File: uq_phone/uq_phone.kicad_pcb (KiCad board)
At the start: 2 copper layers, 113.5 x 110.8 mm, 151 parts, among them J1 USB4105-GF-A, J10 Conn_01x02, J2 S3B-PH-SM4-TB_LF__SN_, J3 20279-001E-03, J4 20279-001E-03, J5 0786463001, J6 503398-1892, J7 Conn_01x02, J8 54132-4062, J9 SJ-3551B-MSMT-TR-67, Q1 MMBT3904, Q2 MMBT3904, Q3 MMBT2907ALT1G, U1 MCP73871-2CCI_ML, U10 TS3A5018RSVR, U11 NAU88C22YG, U2 TPS62162DSGR, U3 BQ27441DRZR-G1A, U4 RC7620_1104625, U5 TXB0108RGYR, U6 TXB0108RGYR, U7 STM32H730VBTx, U8 LSM6DSVTR, U9 DRV2603RUNR

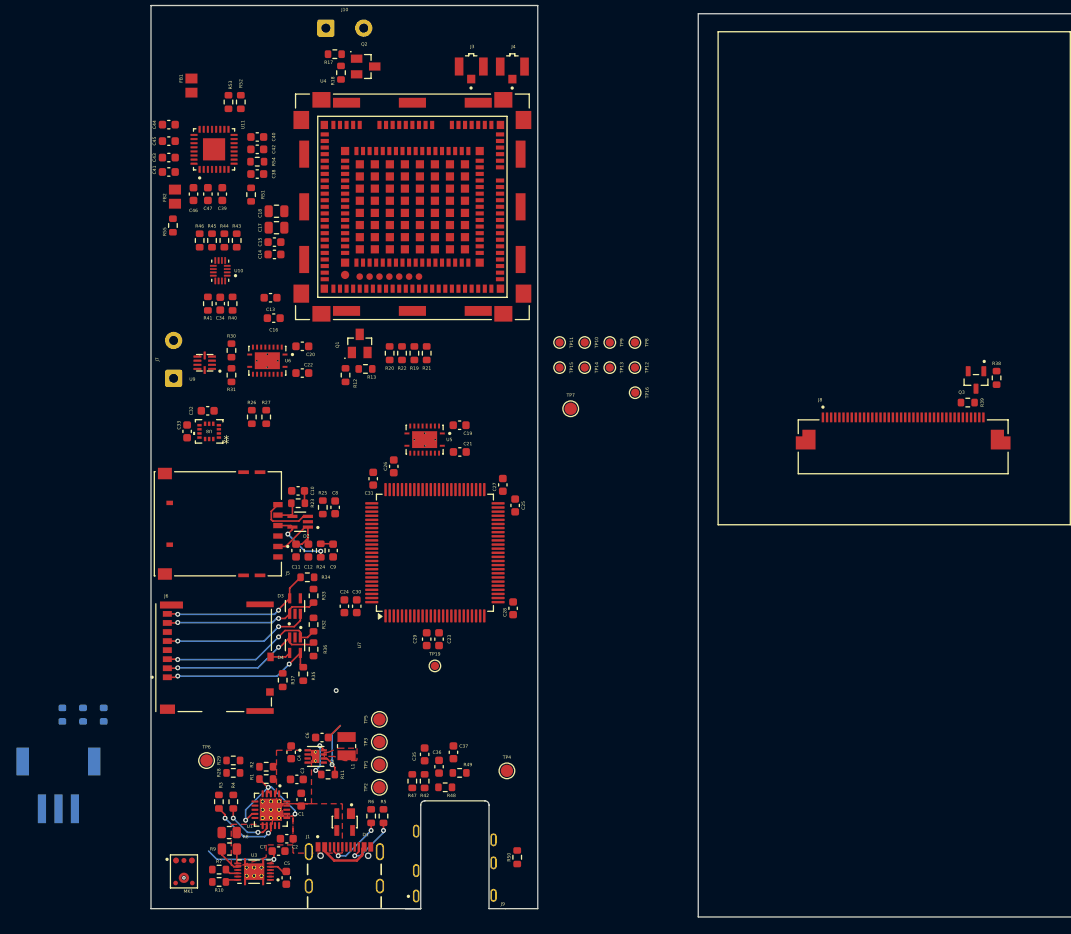
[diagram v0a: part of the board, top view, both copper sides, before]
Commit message: Update LCD, Add Programer, Shrink Footprints
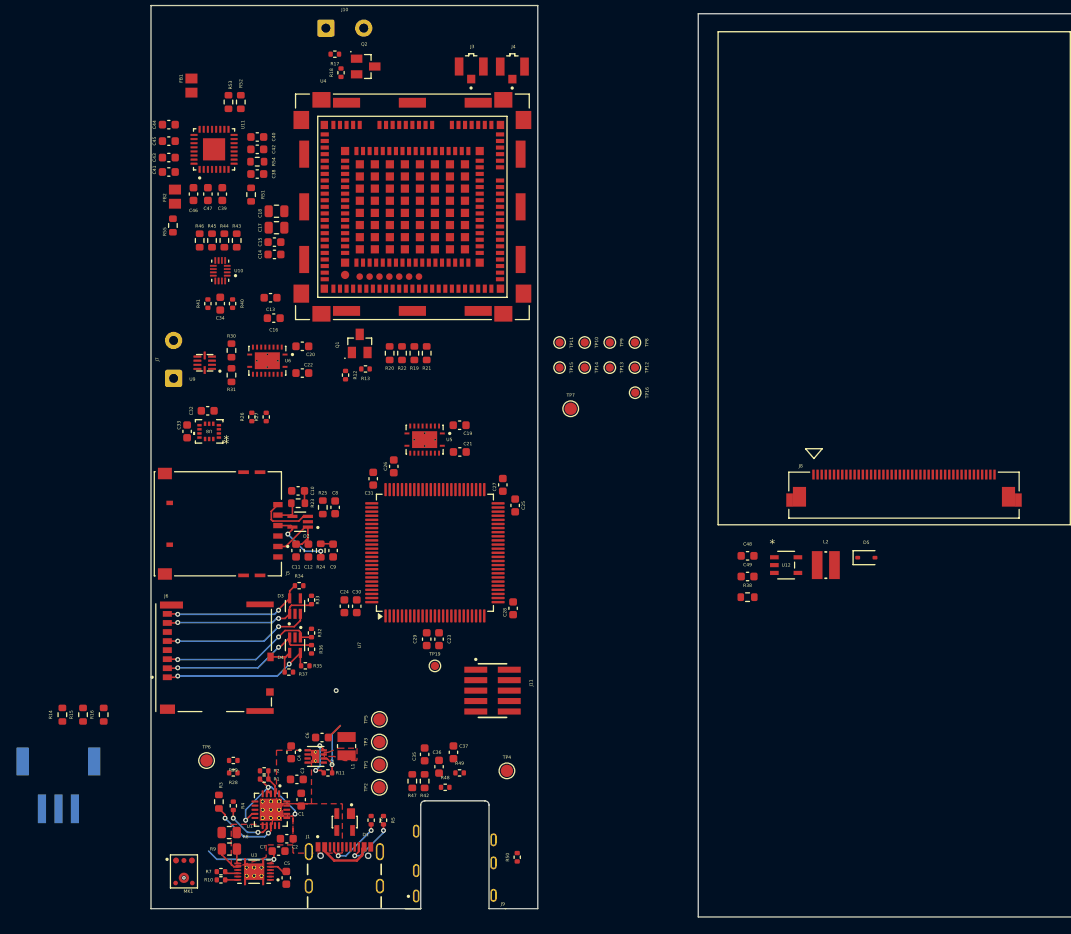
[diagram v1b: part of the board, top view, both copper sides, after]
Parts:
- removed Q3: MMBT2907ALT1G, MMBT2907ALT1G:SOT95P240X111-3N
- removed R39: 0R, Resistor_SMD:R_0603_1608Metric
- added C48: 10uF, Capacitor_SMD:C_0603_1608Metric, F.Cu at (97.7, 129.1)
- added C49: 4.7uF, Capacitor_SMD:C_0603_1608Metric, F.Cu at (97.7, 131.6)
- added D5: PMEG2010EA, Diode_SMD:D_SOD-323, F.Cu at (112.2, 129.3)
- added J11: FTSH-105-XX-X-DV, FTSH-105-XX-X-DV:SAMTEC_FTSH-105-XX-X-DV, F.Cu at (66.8, 145.5)
- added L2: 4.7uH, WE-MAPI_3015:WE-MAPI_3015, F.Cu at (107.2, 130.2)
- added U12: MCP1664T-E/OT, MCP1664T_E_OT:SOT-23-5_OT_MCH, F.Cu at (102.4, 130.2)
- J8: value 54132-4062 -> 541324562; footprint 54132-4062:MOLEX_54132-4062 -> 541324562:CON_541324562_MOL
- R1, R10, R11, R13, R18, R2, R26, R27, R28, R29, R32, R33, R34, R35, R36, R37, R4, R40, R41, R48, R49, R5, R50, R6, R7: footprint Resistor_SMD:R_0603_1608Metric -> Resistor_SMD:R_0402_1005Metric
- R12, R17: value 4k7 -> 4.7k; footprint Resistor_SMD:R_0603_1608Metric -> Resistor_SMD:R_0402_1005Metric
- R14, R15, R16: moved to F.Cu
- R38: value 1k -> 3.83R
- R47: value 2k2 -> 2.2k
- moved R38 40.3 mm to (97.7, 134.1), turned to 0 degrees
- moved J8 9.45 mm to (116.7, 121.7)
- moved R14 5.02 mm to (14.5, 148.4)
- moved R16 5.02 mm to (19.5, 148.4)
- moved R34 1.43 mm to (43.2, 132.8)
- moved R37 1.23 mm to (42.0, 143.2), turned to 0 degrees
- moved R32 1.05 mm to (44.8, 138.5)
- moved R35 1.02 mm to (44.0, 142.5), turned to 0 degrees
- moved R33 0.57 mm to (44.8, 134.5)
- moved R2 0.56 mm to (39.0, 155.2)
- moved R4 0.50 mm to (35.2, 159.5)
- moved R5 0.50 mm to (53.5, 161.2)
- moved R6 0.50 mm to (52.0, 161.2)
- moved R10 0.34 mm to (33.8, 168.5)
- moved R7 0.34 mm to (33.8, 167.5)
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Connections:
- J8 pad 10: DISP_CS -> DISP_WR
- J8 pad 11: DISP_DC -> DISP_RD
- J8 pad 12: DISP_WR -> GND
- J8 pad 13: DISP_RD -> GND
- J8 pad 14: DISP_DB0 -> GND
- J8 pad 15: DISP_DB1 -> GND
- J8 pad 16: DISP_DB2 -> GND
- J8 pad 17: DISP_DB3 -> DISP_DB0
- J8 pad 18: DISP_DB4 -> DISP_DB1
- J8 pad 19: DISP_DB5 -> DISP_DB2
- J8 pad 2: unconnected-(J8-NC-Pad2) -> +3.3V
- J8 pad 20: DISP_DB6 -> DISP_DB3
- J8 pad 21: DISP_DB7 -> DISP_DB4
- J8 pad 22: DISP_DB8 -> DISP_DB5
- J8 pad 23: DISP_DB9 -> DISP_DB6
- J8 pad 24: DISP_DB10 -> DISP_DB7
- J8 pad 25: DISP_DB11 -> DISP_DB8
- J8 pad 26: DISP_DB12 -> DISP_DB9
- J8 pad 27: DISP_DB13 -> DISP_DB10
- J8 pad 28: DISP_DB14 -> DISP_DB11
- J8 pad 29: DISP_DB15 -> DISP_DB12
- J8 pad 3: unconnected-(J8-NC-Pad3) -> +3.3V
- J8 pad 30: DISP_RES -> DISP_DB13
- J8 pad 31: GND -> DISP_DB14
- J8 pad 32: unconnected-(J8-NC-Pad32) -> DISP_DB15
- J8 pad 33: GND -> unconnected-(J8-DB16-Pad33)
- J8 pad 34: GND -> unconnected-(J8-DB17-Pad34)
- J8 pad 35: GND -> unconnected-(J8-SDO-Pad35)
- J8 pad 36: GND -> DISP_LEDA
- J8 pad 37: GND -> DISP_LEDK
- J8 pad 38: Net-(J8-LED-A) -> DISP_LEDK
- J8 pad 39: GND -> DISP_LEDK
- J8 pad 4: unconnected-(J8-NC-Pad4) -> GND
- J8 pad 40: unconnected-(J8-NC-Pad40) -> DISP_LEDK
- J8 pad 5: unconnected-(J8-NC-Pad5) -> GND
- J8 pad 6: unconnected-(J8-NC-Pad6) -> +3.3V
- J8 pad 7: +3.3V -> DISP_RES
- J8 pad 8: +3.3V -> DISP_CS
- J8 pad 9: unconnected-(J8-NC-Pad9) -> DISP_DC
- R38 pad 1: Net-(Q3-Pad1) -> GND
- R38 pad 2: DISP_BL -> DISP_LEDK
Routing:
- net Net-(U1-VPCC): track 0.00 -> 3.12 mm
- net uSD_DET: track 2.53 -> 5.11 mm
- net uSD_DAT1: track 18.9 -> 17.5 mm
- net uSD_CMD: track 20.3 -> 19.7 mm

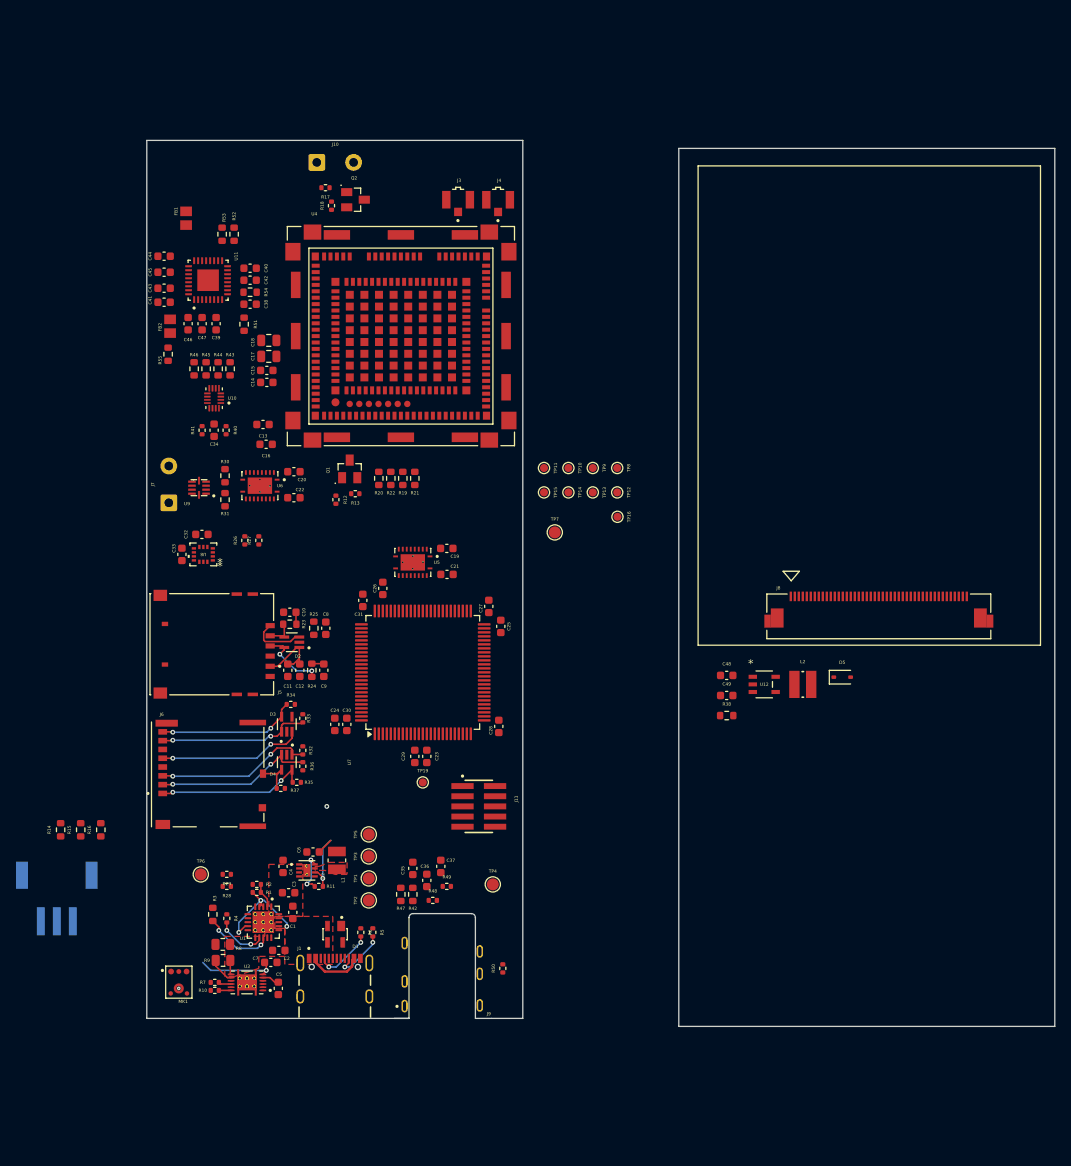
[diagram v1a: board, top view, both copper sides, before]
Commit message: Shrink More footprints, rearragment of PCB
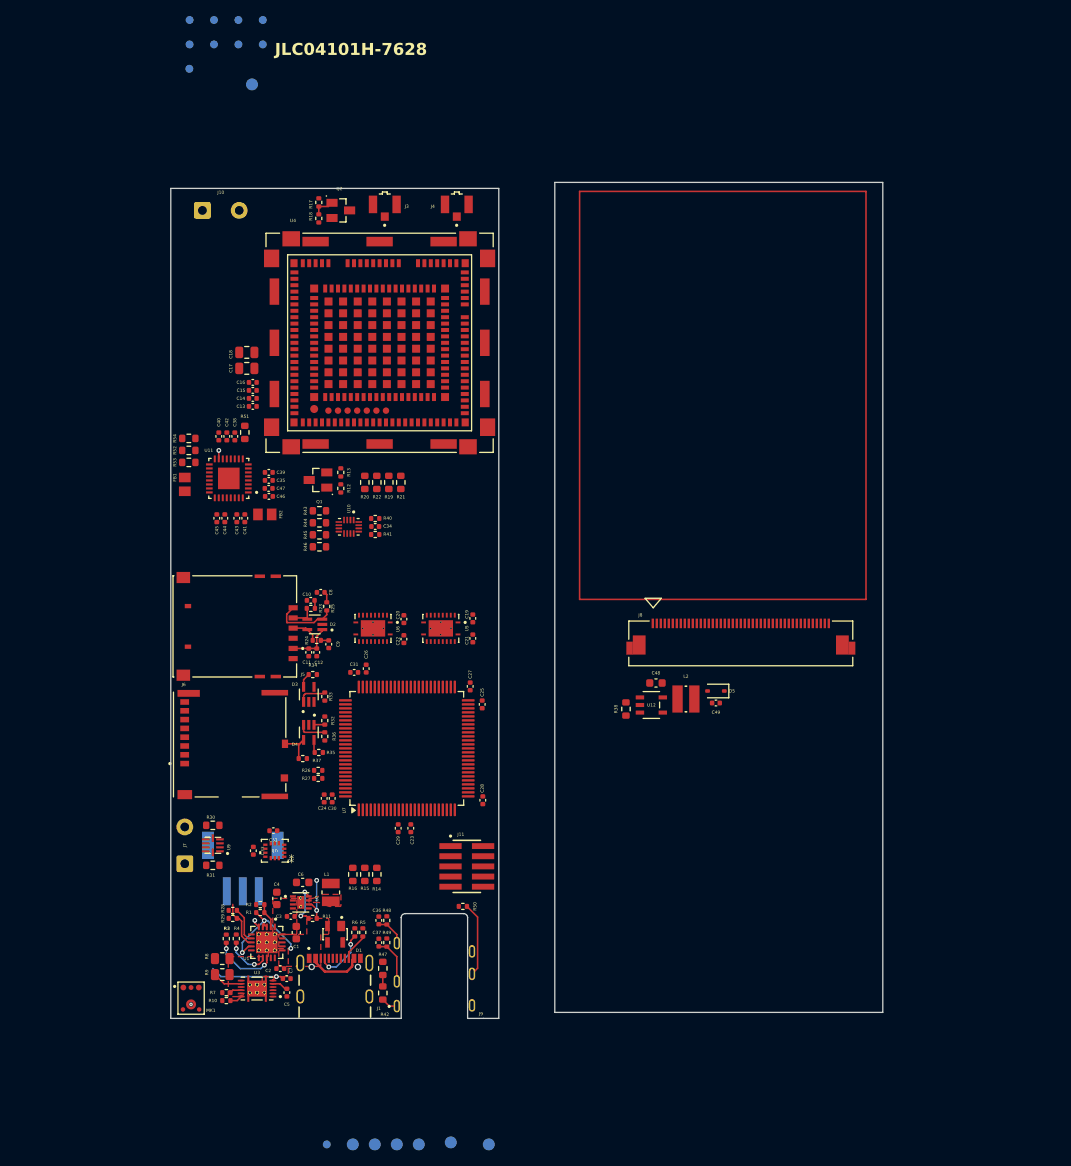
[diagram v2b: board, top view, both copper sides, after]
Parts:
- removed R55: 0R, Resistor_SMD:R_0603_1608Metric
- C10, C11, C12, C13, C14, C15, C16, C19, C2, C20, C21, C22, C23, C24, C25, C26, C27, C28, C29, C3, C30, C31, C32, C33, C34, C35, C36, C37, C38, C39, C40, C41, C42, C43, C44, C45, C46, C47, C49, C5, C7, C8, C9: footprint Capacitor_SMD:C_0603_1608Metric -> Capacitor_SMD:C_0402_1005Metric
- C6: value 1uF -> 22uF
- R23, R24, R25, R3: footprint Resistor_SMD:R_0603_1608Metric -> Resistor_SMD:R_0402_1005Metric
- TP1, TP10, TP11, TP12, TP13, TP14, TP15, TP16, TP19, TP2, TP3, TP4, TP5, TP6, TP7, TP8, TP9: moved to B.Cu
- moved TP16 77.5 mm to (30.6, 53.3)
- moved TP12 77.4 mm to (30.6, 50.2)
- moved TP8 77.4 mm to (30.6, 47.2)
- moved TP13 73.3 mm to (33.6, 50.2)
- moved TP9 73.3 mm to (33.6, 47.2)
- moved TP10 69.6 mm to (36.7, 47.2)
- moved TP14 69.6 mm to (36.7, 50.2)
- moved TP7 67.6 mm to (38.4, 55.2), turned to 180 degrees
- moved TP11 66.1 mm to (39.8, 47.2)
- moved TP15 66.1 mm to (39.8, 50.2)
- moved C35 51.7 mm to (40.5, 104.8), turned to 0 degrees
- moved TP6 49.3 mm to (68.0, 187.8), turned to -90 degrees
- moved TP19 46.8 mm to (47.8, 187.8), turned to -90 degrees
- moved R31 45.7 mm to (33.5, 152.9), turned to 0 degrees
- moved J7 45.2 mm to (30.0, 152.7)
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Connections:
- C38 pad 2: AGND -> GND
- FB2 pad 2: Net-(FB2-Pad2) -> +3.3V
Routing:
- net uSD_CMD: track 19.7 -> 1.36 mm, vias 2 -> 0
- net uSD_CLK: track 18.0 -> 0.00 mm, vias 2 -> 0
- net uSD_DAT2: track 19.0 -> 1.61 mm, vias 2 -> 0
- net uSD_DAT3: track 19.9 -> 3.51 mm, vias 2 -> 0
- net uSD_DAT1: track 17.5 -> 1.81 mm, vias 2 -> 0
- net uSD_DAT0: track 18.9 -> 3.61 mm, vias 2 -> 0
- net HP_DET: track 0.00 -> 10.3 mm, vias 0 -> 1
- net MCP_STAT1: track 0.00 -> 6.10 mm
- net Net-(C37-Pad2): track 0.00 -> 5.87 mm
- net Net-(J5-RST): track 8.53 -> 3.47 mm, vias 2 -> 0
- net MCP_STAT2: track 0.00 -> 4.49 mm
- net Net-(C36-Pad2): track 0.00 -> 3.85 mm
- net Net-(J1-CC2): track 6.94 -> 3.46 mm, vias 2 -> 0
- net +3.3V: track 9.60 -> 6.14 mm
- net SIM_VDD: track 8.46 -> 5.61 mm
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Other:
- board size 113.5 x 110.8 mm -> 89 x 104.5 mm
- copper layers 2 -> 4
- board text added: "JLC04101H-7628"

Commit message: Update PCB, minor changes
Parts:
- added REF**: 8.5mmSnaptron, custom_footprints:8.5mmSnaptron, F.Cu at (112.5, 141.3)
- added REF**: 8.5mmSnaptron, custom_footprints:8.5mmSnaptron, F.Cu at (124.0, 133.2)
- added REF**: 8.5mmSnaptron, custom_footprints:8.5mmSnaptron, F.Cu at (112.5, 158.0)
- added REF**: 8.5mmSnaptron, custom_footprints:8.5mmSnaptron, F.Cu at (118.2, 128.0)
- added REF**: 8.5mmSnaptron, custom_footprints:8.5mmSnaptron, F.Cu at (112.5, 166.0)
- added REF**: 8.5mmSnaptron, custom_footprints:8.5mmSnaptron, F.Cu at (124.0, 122.0)
- added REF**: 8.5mmSnaptron, custom_footprints:8.5mmSnaptron, F.Cu at (185.8, 137.0)
- added REF**: 8.5mmSnaptron, custom_footprints:8.5mmSnaptron, F.Cu at (112.5, 150.0)
- added REF**: 8.5mmSnaptron, custom_footprints:8.5mmSnaptron, F.Cu at (158.0, 141.1)
- added REF**: 8.5mmSnaptron, custom_footprints:8.5mmSnaptron, F.Cu at (124.0, 158.0)
- added REF**: 8.5mmSnaptron, custom_footprints:8.5mmSnaptron, F.Cu at (108.0, 132.8)
- added REF**: 8.5mmSnaptron, custom_footprints:8.5mmSnaptron, F.Cu at (124.0, 150.0)
- added REF**: 8.5mmSnaptron, custom_footprints:8.5mmSnaptron, F.Cu at (174.0, 142.5)
- added REF**: 8.5mmSnaptron, custom_footprints:8.5mmSnaptron, F.Cu at (108.0, 124.2)
- added REF**: 8.5mmSnaptron, custom_footprints:8.5mmSnaptron, F.Cu at (124.0, 166.0)
- added REF**: 8.5mmSnaptron, custom_footprints:8.5mmSnaptron, F.Cu at (136.2, 165.8)
- added REF**: 8.5mmSnaptron, custom_footprints:8.5mmSnaptron, F.Cu at (124.0, 141.3)
- added REF**: 8.5mmSnaptron, custom_footprints:8.5mmSnaptron, F.Cu at (136.2, 149.8)
- added REF**: 8.5mmSnaptron, custom_footprints:8.5mmSnaptron, F.Cu at (136.3, 141.1)
- added REF**: 8.5mmSnaptron, custom_footprints:8.5mmSnaptron, F.Cu at (139.2, 132.8)
- added REF**: 8.5mmSnaptron, custom_footprints:8.5mmSnaptron, F.Cu at (129.8, 127.8)
- added REF**: 8.5mmSnaptron, custom_footprints:8.5mmSnaptron, F.Cu at (136.2, 157.8)
- added REF**: 8.5mmSnaptron, custom_footprints:8.5mmSnaptron, F.Cu at (139.2, 124.2)
- J2: moved to F.Cu
- moved J8 164.1 mm to (-63.3, 104.3)
- moved C48 102.2 mm to (-13.2, 125.5)
- moved C49 101.7 mm to (-5.20, 128.0)
- moved D5 101.7 mm to (-5.20, 126.5)
- moved L2 101.7 mm to (-8.95, 127.5)
- moved U12 101.7 mm to (-13.3, 128.2)
- moved R38 101.5 mm to (-16.2, 128.2)
- moved J5 76.6 mm to (59.5, 50.0), turned to 90 degrees
- moved C11 67.9 mm to (56.2, 59.2), turned to 180 degrees
- moved C12 66.7 mm to (56.2, 60.2), turned to 180 degrees
- moved R24 65.5 mm to (57.7, 60.2), turned to -90 degrees
- moved D2 64.2 mm to (59.7, 60.0), turned to 90 degrees
- moved C9 64.1 mm to (57.3, 61.8), turned to 180 degrees
- moved R23 63.3 mm to (61.7, 59.5), turned to -90 degrees
- moved C10 62.6 mm to (62.7, 59.5), turned to 90 degrees
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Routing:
- net MCP_PG: track 0.00 -> 7.61 mm
- net Net-(J2-VBatt): track 13.7 -> 20.6 mm, vias 1 -> 2
- net MCP_STAT2: track 4.49 -> 9.15 mm
- net MCP_STAT1: track 6.10 -> 10.4 mm
- net Net-(U1-PROG3): track 5.70 -> 9.80 mm
- net USB_N: track 0.00 -> 3.22 mm
- net USB_P: track 0.00 -> 3.22 mm
- net Net-(U1-VPCC): track 3.12 -> 4.22 mm
- added copper zone on F.Cu, net Net-(J2-VBatt)
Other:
- board size 89 x 104.5 mm -> 116 x 105 mm
- board text added: "REF**"

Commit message: Changed SIM/uSD port & adjust routing
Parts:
- removed D2, D3, D4: ESDA6V1W5, ESDA6V1W5:SOT65P210X110-5N
- removed J6: 503398-1892, 503398-1892:MOLEX_503398-1892
- removed R33, R34, R35, R36: 47k, Resistor_SMD:R_0402_1005Metric
- removed R37: 10k, Resistor_SMD:R_0402_1005Metric
- added R39: 10k, Resistor_SMD:R_0402_1005Metric, F.Cu at (42.0, 105.5)
- added U13: TPD3F303DQDR, TPD3F303DQDR:SON40P170X135X80-9N, F.Cu at (44.6, 104.2)
- added U14: TPD8F003DQDR, TPD8F003DQDR:SON40P135X330X80-17N, F.Cu at (30.9, 94.3)
- J10, J7: footprint Connector_Wire:SolderWire-0.5sqmm_1x02_P4.6mm_D0.9mm_OD2.1mm -> Connector_Wire:SolderWire-0.25sqmm_1x02_P4.2mm_D0.65mm_OD1.7mm
- J5: value 0786463001 -> KP15B-6S-SF_800_; footprint Sim_card:MOLEX_0786463001 -> KP15B-6S-SF_800_:HIROSE_KP15B-6S-SF_800_
- R32: value 47k -> 10k
- moved J8 187.9 mm to (124.5, 99.0)
- moved C48 128.0 mm to (113.4, 106.8)
- moved C49 128.0 mm to (121.5, 109.2)
- moved D5 128.0 mm to (121.5, 107.8)
- moved L2 128.0 mm to (117.7, 108.8)
- moved R38 128.0 mm to (110.4, 109.5)
- moved U12 128.0 mm to (113.4, 109.5)
- moved J7 87.4 mm to (80.7, 138.8), turned to 0 degrees
- moved R30 86.2 mm to (83.6, 144.5)
- moved R31 86.2 mm to (83.6, 149.5)
- moved U9 86.2 mm to (83.6, 147.0)
- moved C32 80.0 mm to (83.3, 129.0)
- moved C33 80.0 mm to (80.8, 131.5)
- moved U8 80.0 mm to (83.5, 131.5)
- moved R32 60.5 mm to (28.1, 94.0), turned to -90 degrees
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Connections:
- net Net-(U4A-USB_D+) renamed /Mobile/MOB_USB_P
- net Net-(U4A-USB_D-) renamed /Mobile/MOB_USB_N
- R23 pad 1: Net-(J5-I/O) -> Net-(U13-DATA2_IN)
- R24 pad 1: Net-(J5-RST) -> Net-(U13-DATA1_IN)
- R25 pad 1: Net-(J5-CLK) -> Net-(U13-CLK_IN)
- R32 pad 1: uSD_CMD -> uSD_DET
- U4 pad 64: unconnected-(U4A-UIM1_SIMA_DET-Pad64) -> SIM_DET
- U4 pad P14: (no net) -> GND
- U4 pad P17: (no net) -> GND
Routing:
- net MOB_MAIN_ANT: track 0.00 -> 10.7 mm
- net USB_P: track 3.22 -> 13.1 mm
- net Net-(J5-CLK): track 8.11 -> 0.00 mm
- net USB_N: track 3.22 -> 11.3 mm
- net MOB_AUX_ANT: track 0.00 -> 7.50 mm
- net SIM_VDD: track 5.61 -> 0.00 mm
- net uSD_DET: track 5.11 -> 0.00 mm
- net BAT_THERM: track 1.02 -> 5.94 mm, vias 1 -> 2
- net uSD_DAT0: track 3.61 -> 0.00 mm
- net uSD_DAT3: track 3.51 -> 0.00 mm
- net Net-(J5-RST): track 3.47 -> 0.00 mm
- net Net-(J5-I/O): track 3.21 -> 0.00 mm
- net uSD_DAT1: track 1.81 -> 0.00 mm
- net uSD_DAT2: track 1.61 -> 0.00 mm
- net Net-(U13-DATA2_IN): track 0.00 -> 1.44 mm
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- added copper zone on B.Cu, net GND
- added copper zone on F.Cu, net GND
- added copper zone on In1.Cu, net GND
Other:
- board size 116 x 105 mm -> 116.9 x 105 mm
- board text added: "1.3mm spacing on vias"
- board text added: "Calcs made for JLC04101H-7628(Standard/Finished thickness1.02mm±10%)"
- board text removed: "JLC04101H-7628"
- board text removed: "REF**"
